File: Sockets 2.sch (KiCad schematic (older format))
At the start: 17 parts, among them J18 TABLE SENSOR, J19 PHOTO SENSOR EMITER, J20 PHOTO SENSOR RECEIVER, Q5 BC817, Q6 BC817

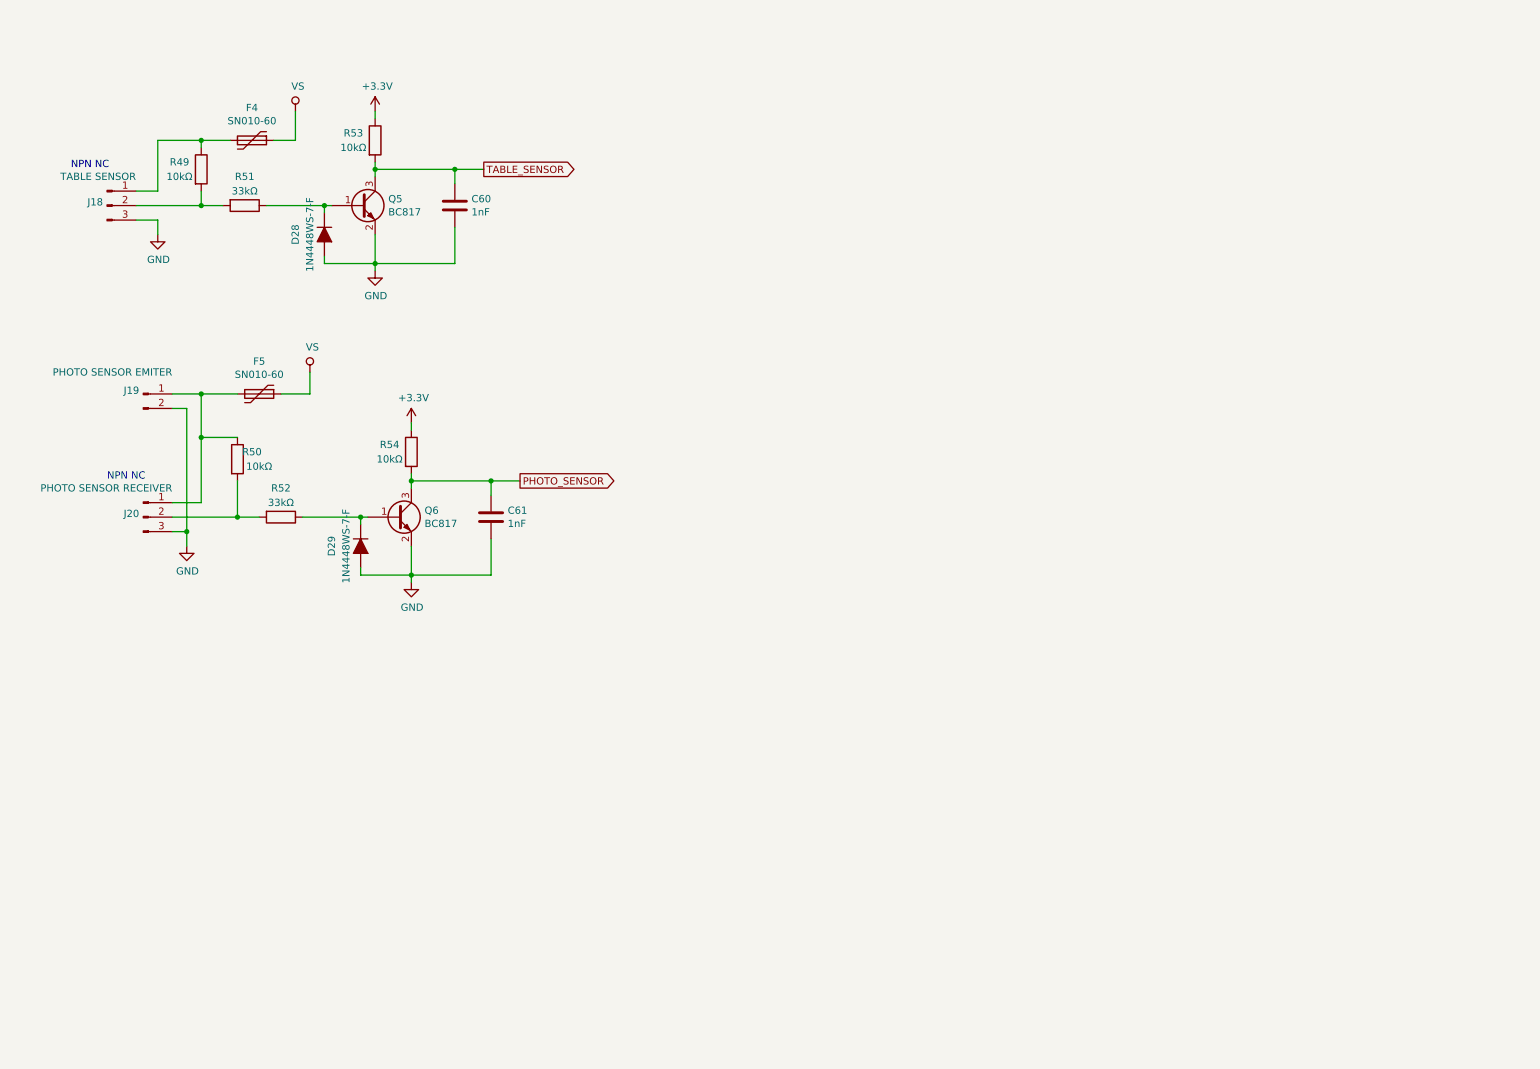
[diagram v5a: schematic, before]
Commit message: Added 12V regulator, aditional input, outputs, improved inputs ESD
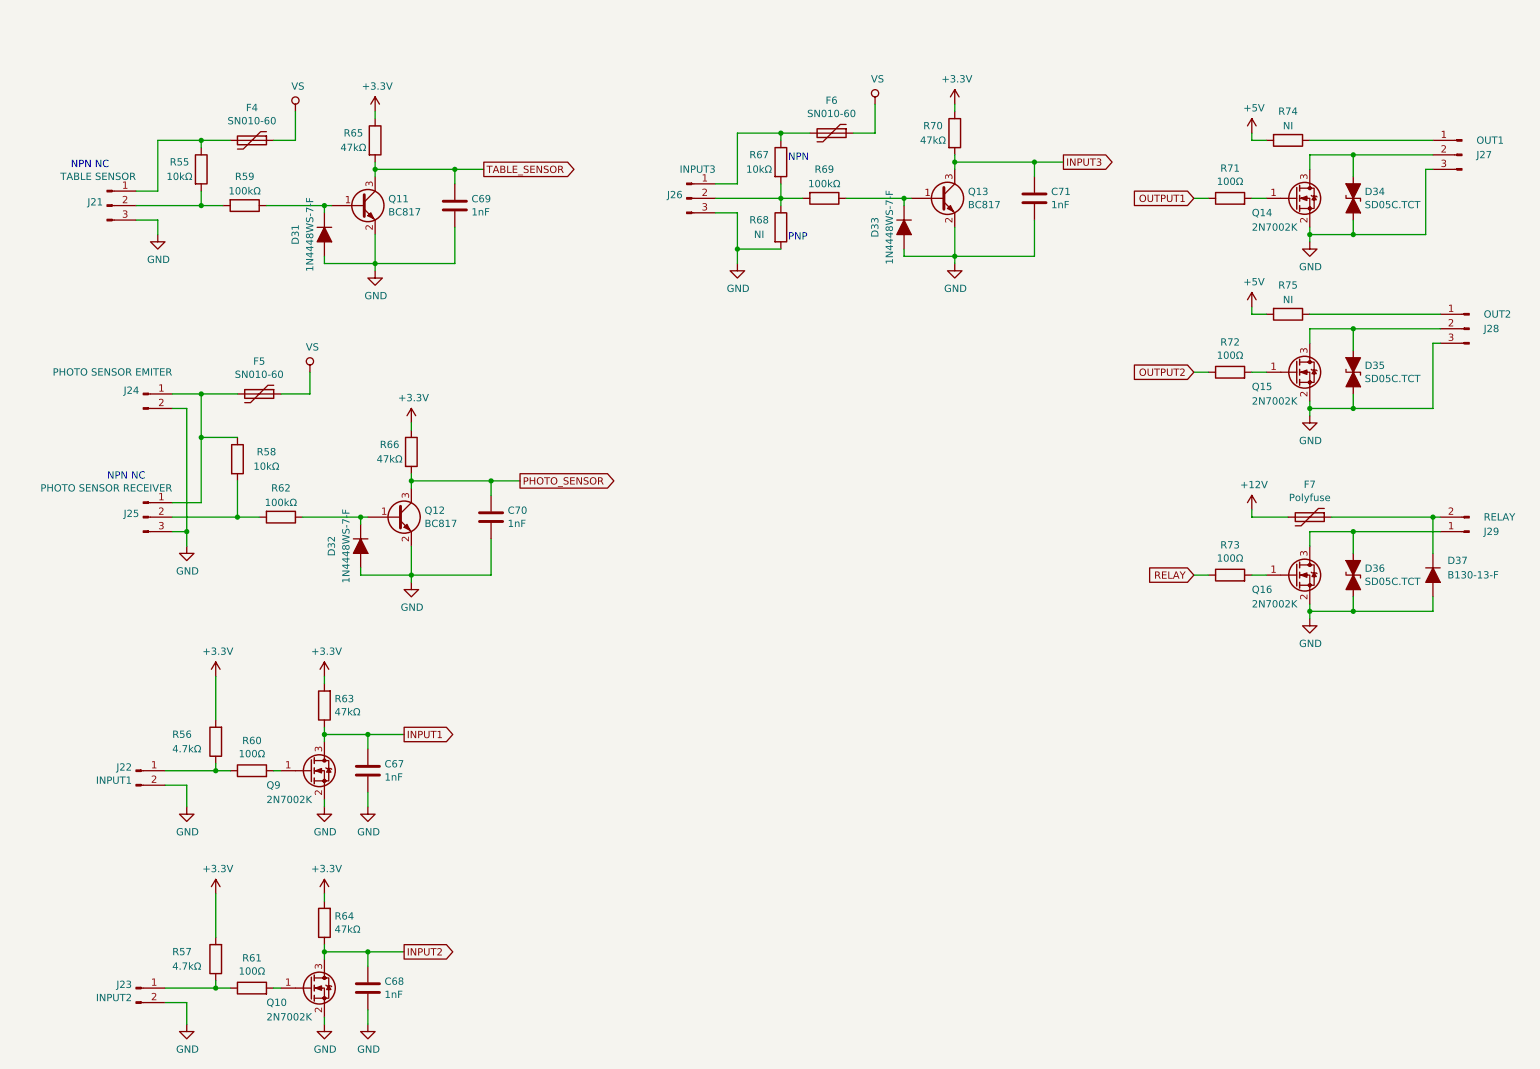
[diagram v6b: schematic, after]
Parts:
- added C67, C68, C71: 1nF, Capacitor_SMD:C_0603_1608Metric, symbol Device:C
- added D33: 1N4448WS-7-F, Diode_SMD:D_SOD-323, symbol Device:D_ALT
- added D34, D35, D36: SD05C.TCT, Diode_SMD:D_SOD-323, symbol Device:D_TVS_ALT
- added D37: B130-13-F, Diode_SMD:D_SMA, symbol Device:D_ALT
- added F6: SN010-60, Fuse:Fuse_1206_3216Metric, symbol Device:Polyfuse
- added F7: Polyfuse, Fuse:Fuse_1206_3216Metric, symbol Device:Polyfuse
- added J22: INPUT1, Connector_JST:JST_PH_B2B-PH-K_1x02_P2.00mm_Vertical, symbol Connector:Conn_01x02_Male
- added J23: INPUT2, Connector_JST:JST_PH_B2B-PH-K_1x02_P2.00mm_Vertical, symbol Connector:Conn_01x02_Male
- added J26: INPUT3, Connector_JST:JST_PH_B3B-PH-K_1x03_P2.00mm_Vertical, symbol Connector:Conn_01x03_Male
- added J27: OUT1, Connector_JST:JST_PH_B3B-PH-K_1x03_P2.00mm_Vertical, symbol Connector:Conn_01x03_Male
- added J28: OUT2, Connector_JST:JST_PH_B3B-PH-K_1x03_P2.00mm_Vertical, symbol Connector:Conn_01x03_Male
- added J29: RELAY, Connector_JST:JST_PH_B2B-PH-K_1x02_P2.00mm_Vertical, symbol Connector:Conn_01x02_Male
- added Q10, Q14, Q15, Q16, Q9: 2N7002K, Package_TO_SOT_SMD:SOT-23, symbol Transistor_FET:2N7002K
- added Q13: BC817, Package_TO_SOT_SMD:SOT-23, symbol Transistor_BJT:BC817
- added R56, R57: 4.7kΩ, Resistor_SMD:R_0603_1608Metric, symbol Device:R
- added R60, R61, R71, R72, R73: 100Ω, Resistor_SMD:R_0603_1608Metric, symbol Device:R
- added R63, R64, R70: 47kΩ, Resistor_SMD:R_0603_1608Metric, symbol Device:R
- added R67: 10kΩ, Resistor_SMD:R_0603_1608Metric, symbol Device:R
- added R68: NI, Resistor_SMD:R_0603_1608Metric, symbol Device:R
- added R69: 100kΩ, Resistor_SMD:R_0603_1608Metric, symbol Device:R
- added R74, R75: NI, Resistor_SMD:R_0805_2012Metric, symbol Device:R
- R59: renamed from R51; value 33kΩ -> 100kΩ
- R62: renamed from R52; value 33kΩ -> 100kΩ
- R65: renamed from R53; value 10kΩ -> 47kΩ
- R66: renamed from R54; value 10kΩ -> 47kΩ
- renumbered C60 to C69, C61 to C70, D28 to D31, D29 to D32, J18 to J21, J19 to J24, J20 to J25, Q5 to Q11, Q6 to Q12, R49 to R55, R50 to R58
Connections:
- net +3V3: now also R56.2, R57.2, R63.2, R64.2, R70.1
- net GND: now also C67.2, C68.2, C71.2, D33.2 (A), D34.2 (A2), D35.2 (A2), D36.2 (A2), D37.2 (A), J22.2 (Pin_2), J23.2 (Pin_2), J26.3 (Pin_3), J27.3 (Pin_3), J28.3 (Pin_3), Q10.2 (S), Q13.2 (E), Q14.2 (S), Q15.2 (S), Q16.2 (S), Q9.2 (S), R68.2
- net VS: now also F6.1
- new net: Q9.1 (G), R60.2
- new net: J22.1 (Pin_1), R56.1, R60.1
- new net: Q10.1 (G), R61.2
- new net: J23.1 (Pin_1), R57.1, R61.1
- new net: F6.2, J26.1 (Pin_1), R67.1
- new net: J26.2 (Pin_2), R67.2, R68.1, R69.2
- new net: D33.1 (K), Q13.1 (B), R69.1
- new net: J27.1 (Pin_1), R74.1
- new net: J28.1 (Pin_1), R75.1
- new net: D34.1 (A1), J27.2 (Pin_2), Q14.3 (D)
- new net: D35.1 (A1), J28.2 (Pin_2), Q15.3 (D)
- new net: Q14.1 (G), R71.2
- new net: Q15.1 (G), R72.2
- new net: D36.1 (A1), J29.1 (Pin_1), Q16.3 (D)
- new net: Q16.1 (G), R73.2
- new net: D37.1 (K), F7.1, J29.2 (Pin_2)
- new net +12V: F7.2
- new net +5V: R74.2, R75.2
- new net INPUT1: C67.1, Q9.3 (D), R63.1
- new net INPUT2: C68.1, Q10.3 (D), R64.1
- new net INPUT3: C71.1, Q13.3 (C), R70.2
- new net OUTPUT1: R71.1
- new net OUTPUT2: R72.1
- new net RELAY: R73.1
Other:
- note added: "NPN"
- note added: "PNP"

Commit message: Added analog input
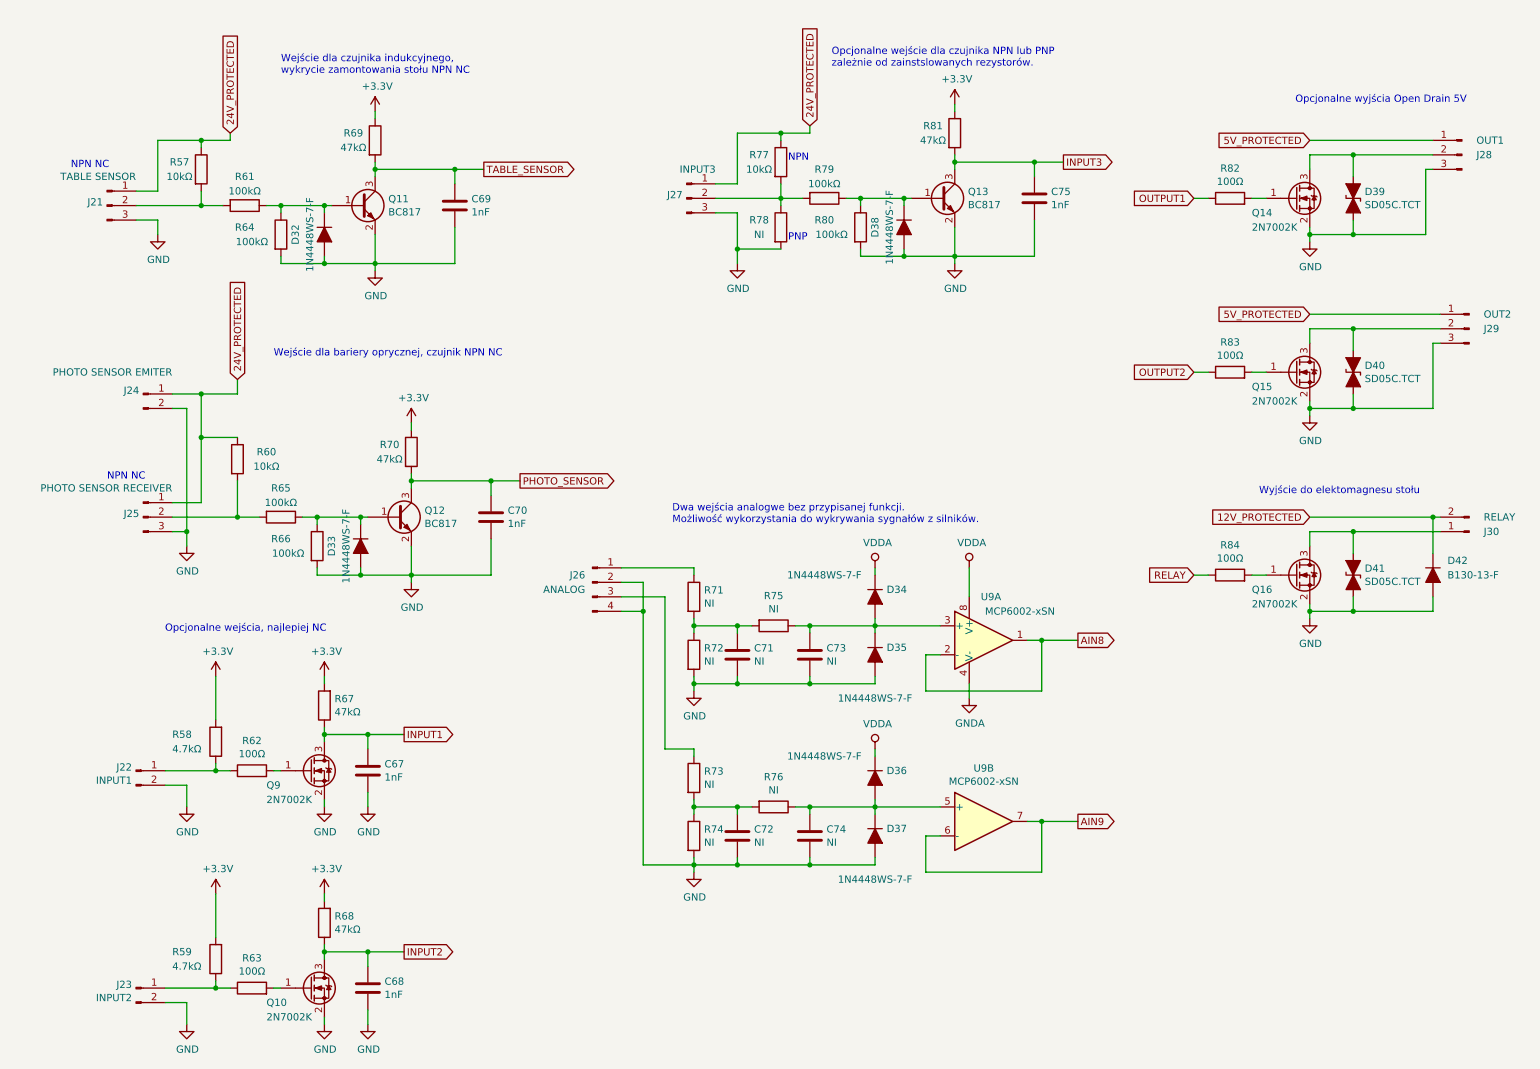
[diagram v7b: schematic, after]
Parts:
- removed F4, F5, F6: SN010-60, Fuse:Fuse_1206_3216Metric, symbol Device:Polyfuse
- removed F7: Polyfuse, Fuse:Fuse_1206_3216Metric, symbol Device:Polyfuse
- added C71, C72, C73, C74: NI, Capacitor_SMD:C_0603_1608Metric, symbol Device:C
- added D34, D35, D36, D37: 1N4448WS-7-F, Diode_SMD:D_SOD-323, symbol Device:D_ALT
- added J26: ANALOG, Connector_JST:JST_PH_B4B-PH-K_1x04_P2.00mm_Vertical, symbol Connector:Conn_01x04_Male
- added R64, R66, R80: 100kΩ, Resistor_SMD:R_0603_1608Metric, symbol Device:R
- added R71, R72, R73, R76: NI, Resistor_SMD:R_0603_1608Metric, symbol Device:R
- added U9: MCP6002-xSN, Package_SO:SOIC-8_3.9x4.9mm_P1.27mm, symbol Amplifier_Operational:MCP6002-xSN
- R74, R75: footprint Resistor_SMD:R_0805_2012Metric -> Resistor_SMD:R_0603_1608Metric; Cena 0.04651 -> (none); Typ SMD -> (none)
- renumbered C71 to C75, D31 to D32, D32 to D33, D33 to D38, D34 to D39, D35 to D40, D36 to D41, D37 to D42, J26 to J27, J27 to J28, J28 to J29, J29 to J30, R55 to R57, R56 to R58, R57 to R59, R58 to R60, R59 to R61, R60 to R62, R61 to R63, R62 to R65, R63 to R67, R64 to R68, R65 to R69, R66 to R70, R67 to R77, R68 to R78, R69 to R79, R70 to R81, R71 to R82, R72 to R83, R73 to R84
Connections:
- net GND: now also R74.2, C71.2, C72.2, C73.2, C74.2, D35.2 (A), D37.2 (A), J26.2 (Pin_2), J26.4 (Pin_4), R64.2, R66.2, R72.2, R80.2
- net 24V_PROTECTED: now reaches J21.1 (Pin_1), R57.1
- net 24V_PROTECTED: now also J24.1 (Pin_1), J25.1 (Pin_1), J27.1 (Pin_1), R60.1, R77.1
- net at D32.1 (K), Q11.1 (B), R61.1: now also R64.1
- net at D33.1 (K), Q12.1 (B), R65.1: now also R66.1
- net at D38.1 (K), Q13.1 (B), R79.1: now also R80.1
- net at R74.1: now also C72.1, R73.2, R76.2; no longer J28.1 (Pin_1)
- net at R75.1: now also C73.1, D34.2 (A), D35.1 (K), U9.3 (+); no longer J29.1 (Pin_1)
- net 12V_PROTECTED: now reaches D42.1 (K), J30.2 (Pin_2)
- net +5V: no longer names the net of R75.2
- net +5V: now also C71.1, R71.2, R72.1; no longer R74.2
- new net: J26.1 (Pin_1), R71.1
- new net: J26.3 (Pin_3), R73.1
- new net: C74.1, D36.2 (A), D37.1 (K), R76.1, U9.5 (+)
- new net 5V_PROTECTED: J28.1 (Pin_1), J29.1 (Pin_1)
- new net AIN8: U9.1, U9.2 (-)
- new net AIN9: U9.6 (-), U9.7
- new net GNDA: U9.4 (V-)
- new net VDDA: D34.1 (K), D36.1 (K), U9.8 (V+)
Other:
- note added: "Dwa wejścia analogwe bez przypisanej funkcji.\nMożliwość wykorzystania do wykrywania sygnałów z silników."
- note added: "Opcjonalne wejścia, najlepiej NC"
- note added: "Opcjonalne wejście dla czujnika NPN lub PNP\nzależnie od zainstslowanych rezystorów."
- note added: "Opcjonalne wyjścia Open Drain 5V"
- note added: "Wejście dla bariery oprycznej, czujnik NPN NC"
- note added: "Wejście dla czujnika indukcyjnego,\nwykrycie zamontowania stołu NPN NC"
- note added: "Wyjście do elektomagnesu stołu"

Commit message: Improve ESD Protection for TMC2209, Fuses. Schematic ready v1
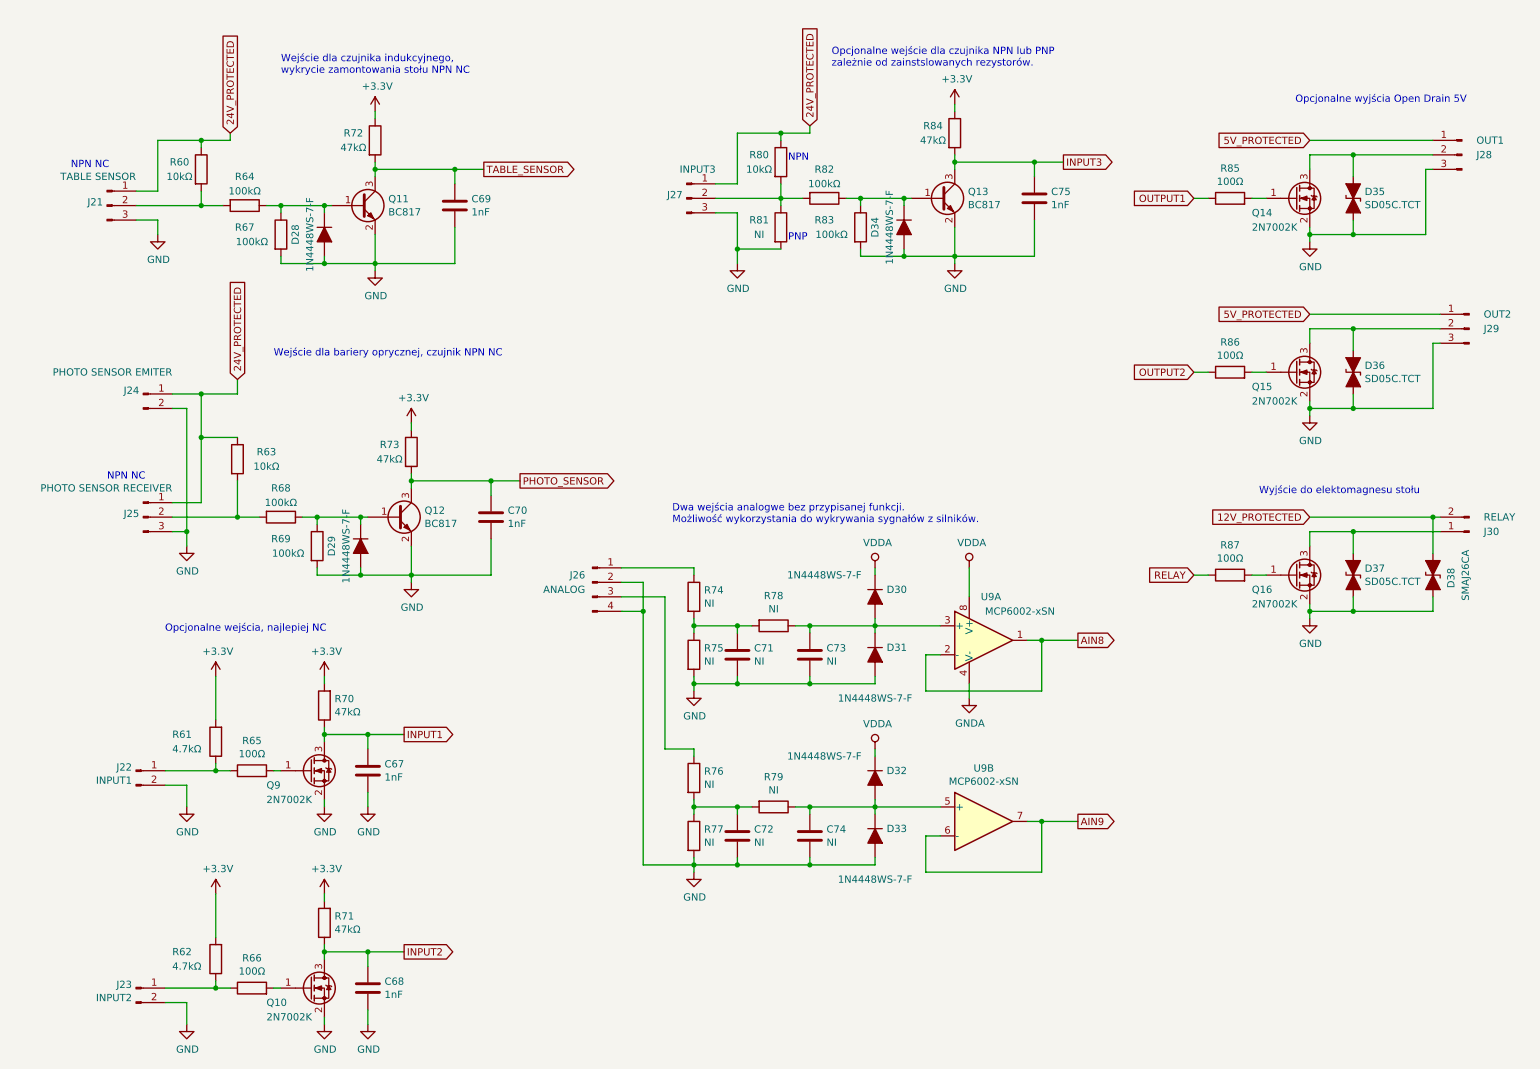
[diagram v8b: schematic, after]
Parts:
- removed D42: B130-13-F, Diode_SMD:D_SMA, symbol Device:D_ALT
- added D38: SMAJ26CA, Diode_SMD:D_SMA, symbol Device:D_TVS_ALT
- renumbered D32 to D28, D33 to D29, D34 to D30, D35 to D31, D36 to D32, D37 to D33, D38 to D34, D39 to D35, D40 to D36, D41 to D37, R57 to R60, R58 to R61, R59 to R62, R60 to R63, R61 to R64, R62 to R65, R63 to R66, R64 to R67, R65 to R68, R66 to R69, R67 to R70, R68 to R71, R69 to R72, R70 to R73, R71 to R74, R72 to R75, R73 to R76, R74 to R77, R75 to R78, R76 to R79, R77 to R80, R78 to R81, R79 to R82, R80 to R83, R81 to R84, R82 to R85, R83 to R86, R84 to R87
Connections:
- net 12V_PROTECTED: now also D38.1 (A1)
- net GND: now also D38.2 (A2)
